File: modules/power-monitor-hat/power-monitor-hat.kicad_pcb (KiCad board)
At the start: 2 copper layers, 65 x 56 mm, 56 parts, among them J1 Barrel_Jack_Switch, J2 GPIO, J3 OutputTerminal, J4 OutputTerminal, J5 OutputTerminal, Q1 BC856BDW1, Q2 SI2301CDS, U1 NCP1117-3.3_SOT223, U2 CAT24C256, U3 INA219AxD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

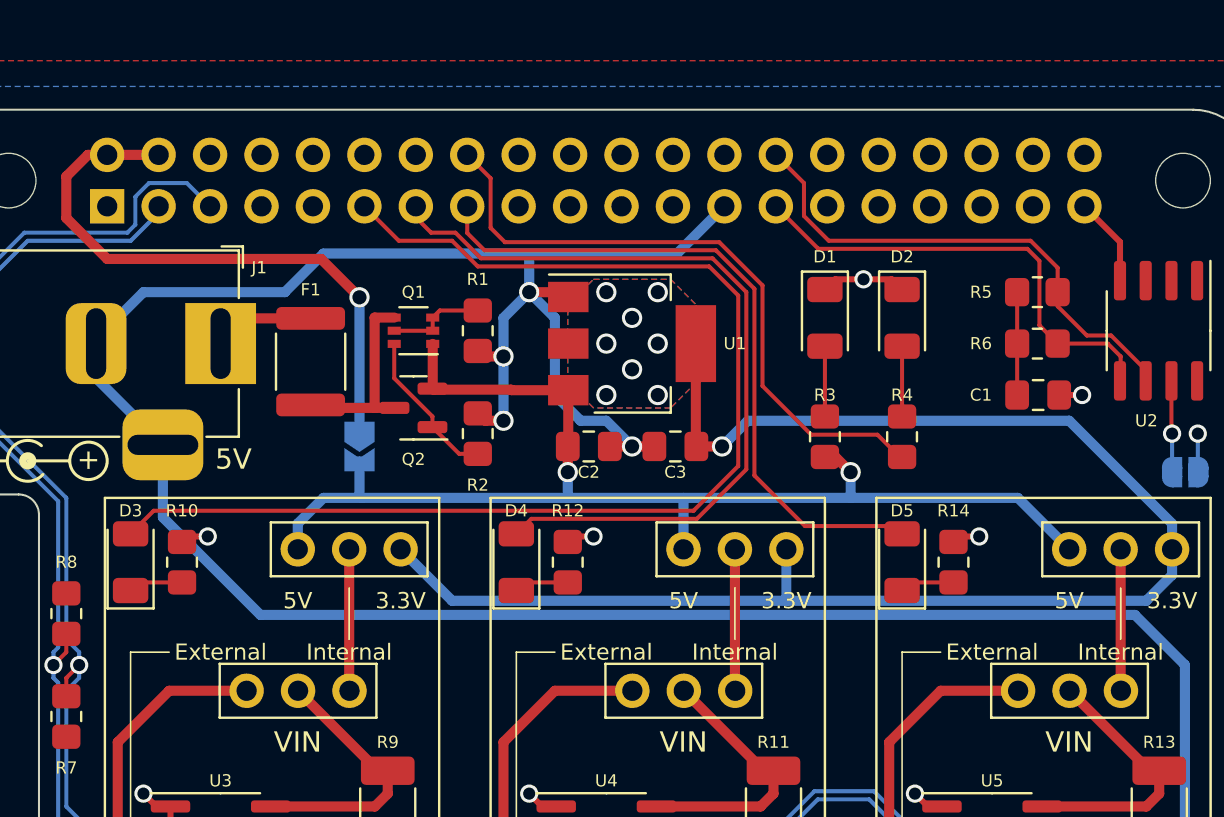
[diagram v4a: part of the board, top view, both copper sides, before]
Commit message: Remove top LED, connect channel LEDs to VIN, expose RX/TX header
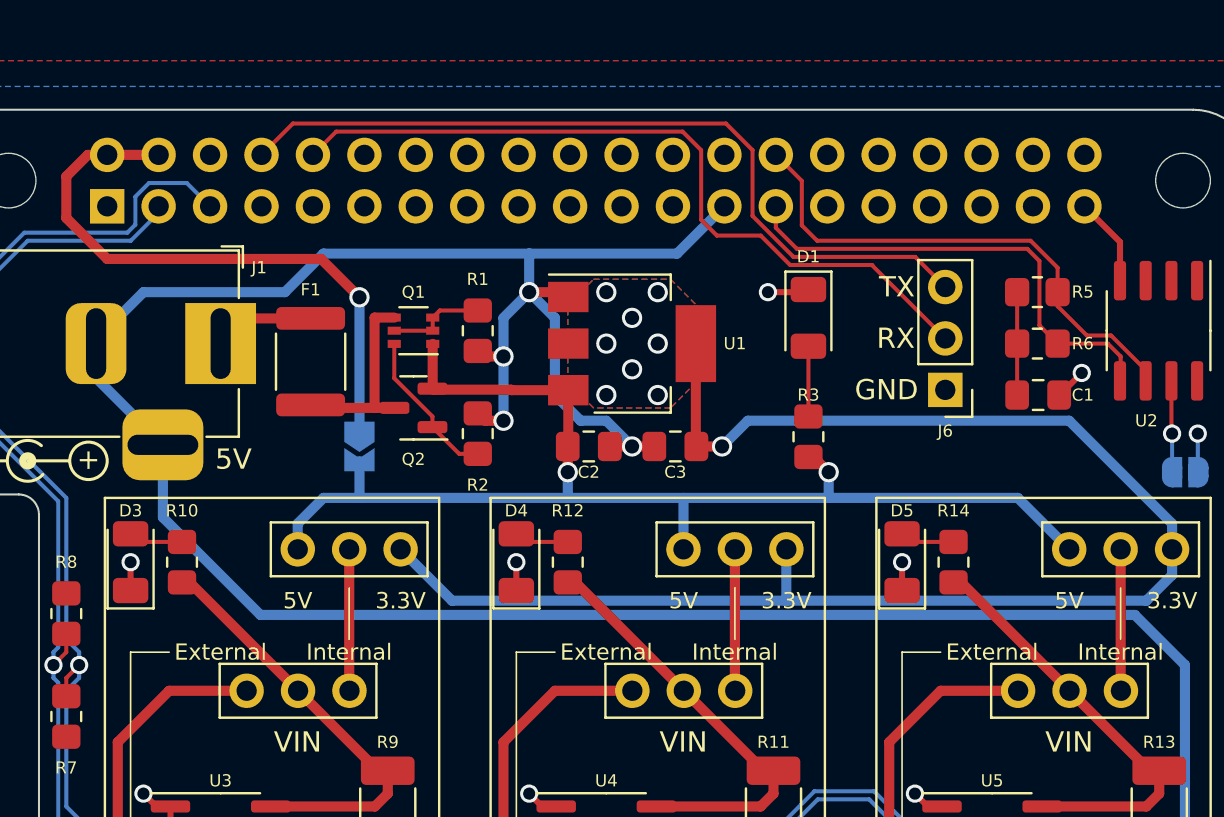
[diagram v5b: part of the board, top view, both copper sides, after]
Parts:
- removed D2: LED, LED_SMD:LED_1206_3216Metric
- removed R4: 470R, Resistor_SMD:R_0805_2012Metric_Pad1.20x1.40mm_HandSolder
- removed SYM2: OSHW-Logo2_9.8x8mm_SilkScreen, Symbol:OSHW-Logo2_9.8x8mm_SilkScreen
- removed SYM3: KiCad-Logo2_6mm_SilkScreen, Symbol:KiCad-Logo2_6mm_SilkScreen
- added J6: Conn_01x03, Connector_PinHeader_2.54mm:PinHeader_1x03_P2.54mm_Vertical, F.Cu at (149.8, 57.8)
- R10, R12, R14: value 470R -> 2kR
- moved D1 0.81 mm to (143.0, 54.3)
- moved R3 0.81 mm to (143.0, 60.1)
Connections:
- D3 pad 1: Net-(D3-Pad1) -> GND
- D3 pad 2: /LED_CH1 -> Net-(R10-Pad1)
- D4 pad 1: Net-(D4-Pad1) -> GND
- D4 pad 2: /LED_CH2 -> Net-(R12-Pad1)
- D5 pad 1: Net-(D5-Pad1) -> GND
- D5 pad 2: /LED_CH3 -> Net-(R14-Pad1)
- J2 pad 10: unconnected-(J2-Pad10) -> /RX
- J2 pad 11: /LED_CH1 -> unconnected-(J2-Pad11)
- J2 pad 13: /LED_CH2 -> unconnected-(J2-Pad13)
- J2 pad 15: /LED_CH3 -> unconnected-(J2-Pad15)
- J2 pad 16: /LED -> unconnected-(J2-Pad16)
- J2 pad 8: unconnected-(J2-Pad8) -> /TX
- R10 pad 1: GND -> Net-(R10-Pad1)
- R10 pad 2: Net-(D3-Pad1) -> /PowerChannel 1/VIN
- R12 pad 1: GND -> Net-(R12-Pad1)
- R12 pad 2: Net-(D4-Pad1) -> /PowerChannel 2/VIN
- R14 pad 1: GND -> Net-(R14-Pad1)
- R14 pad 2: Net-(D5-Pad1) -> /PowerChannel 3/VIN
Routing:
- net /LED_CH1: track 60.1 -> 0.00 mm
- net /TX: track 0.00 -> 39.7 mm
- net /LED_CH2: track 39.3 -> 0.00 mm
- net /RX: track 0.00 -> 38.0 mm
- net /LED_CH3: track 34.3 -> 0.00 mm
- net /LED: track 31.9 -> 0.00 mm
- net /PowerChannel 3/VIN: track 13.2 -> 21.2 mm
- net /PowerChannel 1/VIN: track 13.2 -> 21.2 mm
- net /PowerChannel 2/VIN: track 13.2 -> 21.2 mm
- net Net-(D2-Pad2): track 3.47 -> 0.00 mm
- net Net-(R12-Pad1): track 0.00 -> 2.71 mm
- net Net-(R10-Pad1): track 0.00 -> 2.71 mm
- net Net-(R14-Pad1): track 0.00 -> 2.71 mm
- net Net-(D4-Pad1): track 2.14 -> 0.00 mm
- net Net-(D3-Pad1): track 2.14 -> 0.00 mm
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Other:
- board text added: "RX"
- board text added: "TX"
